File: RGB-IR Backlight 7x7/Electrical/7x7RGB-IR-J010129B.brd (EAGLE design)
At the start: 228.3 x 177.3 mm, 485 parts, among them P4 CON2X3, Q1 NPN_DUAL, Q10 NPN_DUAL, Q11 NPN_DUAL, Q12 NPN_DUAL, Q2 NPN_DUAL, Q3 NPN_DUAL, Q4 NPN_DUAL, Q5 NPN_DUAL, Q6 NPN_DUAL, Q7 NPN_DUAL, Q8 NPN_DUAL, Q9 NPN_DUAL, U1 AP8802, U2 AP8802, U3 AP8802, U4 AP8802

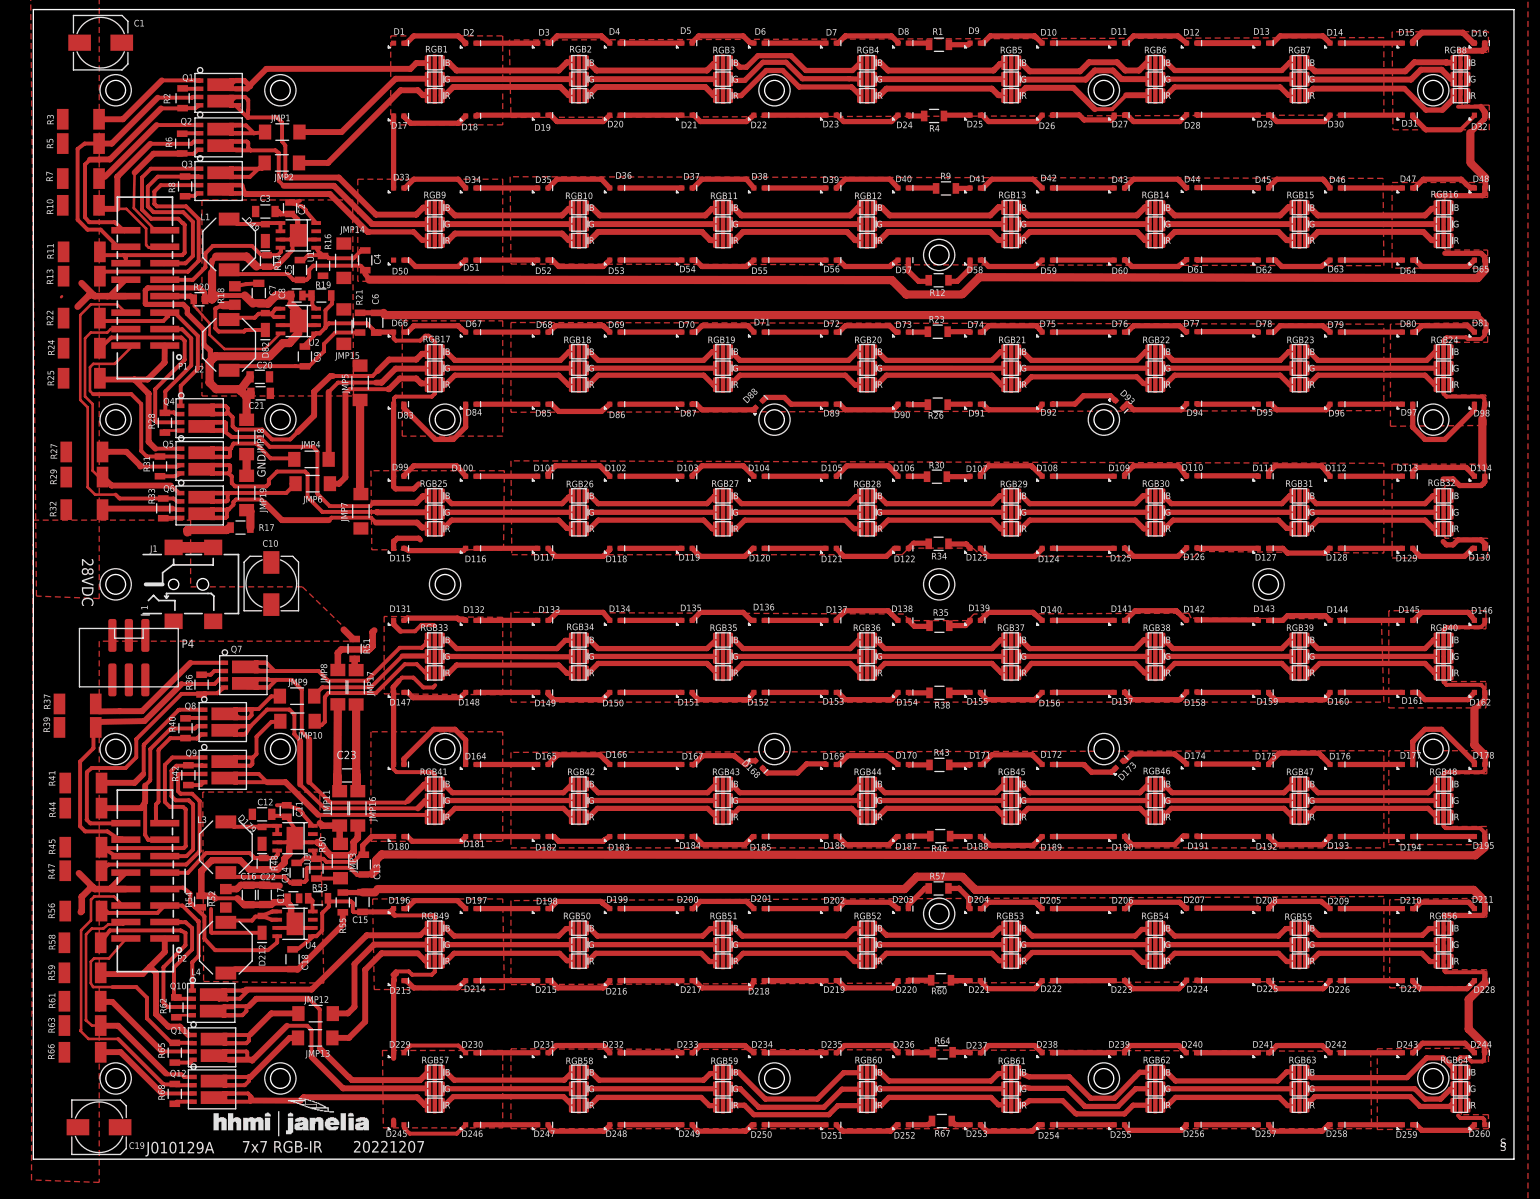
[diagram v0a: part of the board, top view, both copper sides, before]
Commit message: Add 7x7 RGB files
Add current PCB and cable assembly files for 7x7 RGB panel
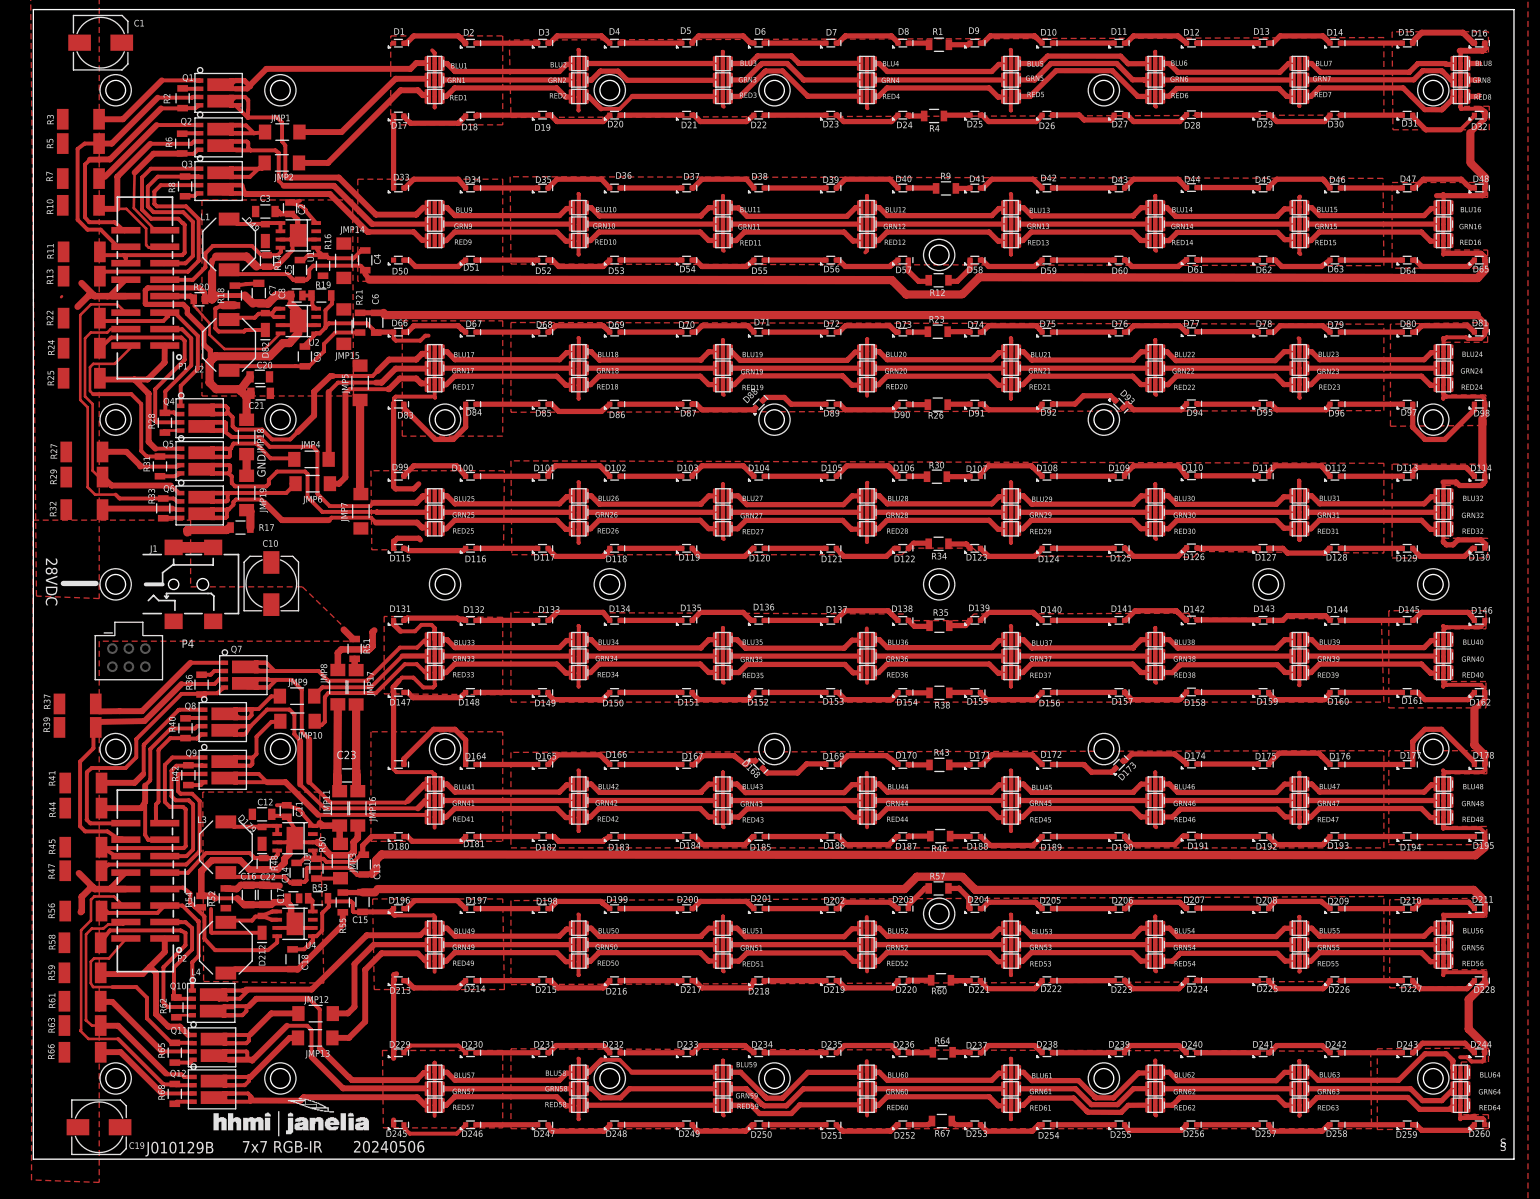
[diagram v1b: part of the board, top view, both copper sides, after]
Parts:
- removed RGB1, RGB10, RGB11, RGB12, RGB13, RGB14, RGB15, RGB16, RGB17, RGB18, RGB19, RGB2, RGB20, RGB21, RGB22, RGB23, RGB24, RGB25, RGB26, RGB27, RGB28, RGB29, RGB3, RGB30, RGB31, RGB32, RGB33, RGB34, RGB35, RGB36, RGB37, RGB38, RGB39, RGB4, RGB40, RGB41, RGB42, RGB43, RGB44, RGB45, RGB46, RGB47, RGB48, RGB49, RGB5, RGB50, RGB51, RGB52, RGB53, RGB54, RGB55, RGB56, RGB57, RGB58, RGB59, RGB6, RGB60, RGB61, RGB62, RGB63, RGB64, RGB7, RGB8, RGB9: LED_RGB_PADSUNPLUS, STEVES_BU:SUNPLUS_RGB
- added BLU1, BLU10, BLU11, BLU12, BLU13, BLU14, BLU15, BLU16, BLU17, BLU18, BLU19, BLU2, BLU20, BLU21, BLU22, BLU23, BLU24, BLU25, BLU26, BLU27, BLU28, BLU29, BLU3, BLU30, BLU31, BLU32, BLU33, BLU34, BLU35, BLU36, BLU37, BLU38, BLU39, BLU4, BLU40, BLU41, BLU42, BLU43, BLU44, BLU45, BLU46, BLU47, BLU48, BLU49, BLU5, BLU50, BLU51, BLU52, BLU53, BLU54, BLU55, BLU56, BLU57, BLU58, BLU59, BLU6, BLU60, BLU61, BLU62, BLU63, BLU64, BLU7, BLU8, BLU9: SP-BLU, RGB_IR_J010131revC:SUNPLUS-LED
- added GRN1, GRN10, GRN11, GRN12, GRN13, GRN14, GRN15, GRN16, GRN17, GRN18, GRN19, GRN2, GRN20, GRN21, GRN22, GRN23, GRN24, GRN25, GRN26, GRN27, GRN28, GRN29, GRN3, GRN30, GRN31, GRN32, GRN33, GRN34, GRN35, GRN36, GRN37, GRN38, GRN39, GRN4, GRN40, GRN41, GRN42, GRN43, GRN44, GRN45, GRN46, GRN47, GRN48, GRN49, GRN5, GRN50, GRN51, GRN52, GRN53, GRN54, GRN55, GRN56, GRN57, GRN58, GRN59, GRN6, GRN60, GRN61, GRN62, GRN63, GRN64, GRN7, GRN8, GRN9: SP-GRN, RGB_IR_J010131revC:SUNPLUS-LED
- added RED1, RED10, RED11, RED12, RED13, RED14, RED15, RED16, RED17, RED18, RED19, RED2, RED20, RED21, RED22, RED23, RED24, RED25, RED26, RED27, RED28, RED29, RED3, RED30, RED31, RED32, RED33, RED34, RED35, RED36, RED37, RED38, RED39, RED4, RED40, RED41, RED42, RED43, RED44, RED45, RED46, RED47, RED48, RED49, RED5, RED50, RED51, RED52, RED53, RED54, RED55, RED56, RED57, RED58, RED59, RED6, RED60, RED61, RED62, RED63, RED64, RED7, RED8, RED9: SP-RED, RGB_IR_J010131revC:SUNPLUS-LED
- added S29, S30, S31, S32: SCREW, STEVES_BU:4-40SOCKET
- P4: device STEVES_BU:2X3_SHROUDED_SMT -> STEVES_BU:2X3_PLUG
- R17, R21: value (none) -> 0R0
- R18, R52: device resistor:R1206 -> STEVES_BU:1206S
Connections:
- removed net N$343: C6.2, D114.C, D130.C, D81.C, D98.C, R21.2, RGB24.T, RGB32.T
- removed net N$413: RGB60.RA, RGB61.RC
- removed net N$417: RGB57.BA, RGB58.BC
- removed net N$418: RGB58.BA, RGB59.BC
- removed net N$419: RGB59.BA, RGB60.BC
- removed net N$420: RGB60.BA, RGB61.BC
- removed net N$421: RGB61.BA, RGB62.BC
- removed net N$422: RGB62.BA, RGB63.BC
- new net IR_RET2: BLU24.T, BLU32.T, C6.2, D114.C, D130.C, D81.C, D98.C, GRN24.T, GRN32.T, R21.2, RED24.T, RED32.T
- new net N$262: RED34.GA, RED35.GC
- new net N$267: RED33.GA, RED34.GC
- new net N$28: GRN5.GA, GRN6.GC
- new net N$292: BLU33.GA, BLU34.GC
- new net N$357: GRN46.GA, GRN47.GC
- new net N$403: RED61.GA, RED62.GC
- new net N$410: BLU59.GA, BLU60.GC
- net BLU1K: now also BLU1.GC; no longer RGB1.BC
- net BLU1K2: now also BLU9.GC; no longer RGB9.BC
- net BLU2K1: now also BLU17.GC; no longer RGB17.BC
- net BLU2K2: now also BLU25.GC; no longer RGB25.BC
- net BLU3K: now also BLU33.GC; no longer RGB33.BC
- net GRN1K: now also GRN1.GC; no longer RGB1.GC
- net GRN1K2: now also GRN9.GC; no longer RGB9.GC
- net GRN2K1: now also GRN17.GC; no longer RGB17.GC
- net GRN2K2: now also GRN25.GC; no longer RGB25.GC
- net GRN3K: now also GRN33.GC; no longer RGB33.GC
- net GULA_1: now also GRN57.GC; no longer RGB57.GC
- net GULA_2: now also RED57.GC; no longer RGB57.RC
- net GULA_3: now also GRN41.GC; no longer RGB41.GC
- net GULA_4: now also RED41.GC; no longer RGB41.RC
- net HS1: now also BLU2.T, BLU3.T, BLU4.T, BLU5.T, BLU6.T, BLU7.T, GRN2.T, GRN3.T, GRN4.T, GRN5.T, GRN6.T, GRN7.T, RED2.T, RED3.T, RED4.T, RED5.T, RED6.T, RED7.T; no longer RGB2.T, RGB3.T, RGB4.T, RGB5.T, RGB6.T, RGB7.T
- net HS2: now also BLU10.T, BLU11.T, BLU12.T, BLU13.T, BLU14.T, BLU15.T, GRN10.T, GRN11.T, GRN12.T, GRN13.T, GRN14.T, GRN15.T, RED10.T, RED11.T, RED12.T, RED13.T, RED14.T, RED15.T; no longer RGB10.T, RGB11.T, RGB12.T, RGB13.T, RGB14.T, RGB15.T
- net HS3: now also BLU18.T, BLU19.T, BLU20.T, BLU21.T, BLU22.T, BLU23.T, GRN18.T, GRN19.T, GRN20.T, GRN21.T, GRN22.T, GRN23.T, RED18.T, RED19.T, RED20.T, RED21.T, RED22.T, RED23.T; no longer RGB18.T, RGB19.T, RGB20.T, RGB21.T, RGB22.T, RGB23.T
- net HS4: now also BLU26.T, BLU27.T, BLU28.T, BLU29.T, BLU30.T, BLU31.T, GRN26.T, GRN27.T, GRN28.T, GRN29.T, GRN30.T, GRN31.T, RED26.T, RED27.T, RED28.T, RED29.T, RED30.T, RED31.T; no longer RGB26.T, RGB27.T, RGB28.T, RGB29.T, RGB30.T, RGB31.T
- net HS5: now also BLU34.T, BLU35.T, BLU36.T, BLU37.T, BLU38.T, BLU39.T, GRN34.T, GRN35.T, GRN36.T, GRN37.T, GRN38.T, GRN39.T, RED34.T, RED35.T, RED36.T, RED37.T, RED38.T, RED39.T; no longer RGB34.T, RGB35.T, RGB36.T, RGB37.T, RGB38.T, RGB39.T
- net HS6: now also BLU42.T, BLU43.T, BLU44.T, BLU45.T, BLU46.T, BLU47.T, GRN42.T, GRN43.T, GRN44.T, GRN45.T, GRN46.T, GRN47.T, RED42.T, RED43.T, RED44.T, RED45.T, RED46.T, RED47.T; no longer RGB42.T, RGB43.T, RGB44.T, RGB45.T, RGB46.T, RGB47.T
- net HS7: now also BLU50.T, BLU51.T, BLU52.T, BLU53.T, BLU54.T, BLU55.T, GRN50.T, GRN51.T, GRN52.T, GRN53.T, GRN54.T, GRN55.T, RED50.T, RED51.T, RED52.T, RED53.T, RED54.T, RED55.T; no longer RGB50.T, RGB51.T, RGB52.T, RGB53.T, RGB54.T, RGB55.T
- net HS8: now also BLU58.T, BLU59.T, BLU60.T, BLU61.T, BLU62.T, BLU63.T, GRN58.T, GRN59.T, GRN60.T, GRN61.T, GRN62.T, GRN63.T, RED58.T, RED59.T, RED60.T, RED61.T, RED62.T, RED63.T; no longer RGB58.T, RGB59.T, RGB60.T, RGB61.T, RGB62.T, RGB63.T
- net IR_DRV3: now also BLU33.T, BLU41.T, GRN33.T, GRN41.T, RED33.T, RED41.T; no longer RGB33.T, RGB41.T
- net IR_DRV4: now also BLU49.T, BLU57.T, GRN49.T, GRN57.T, RED49.T, RED57.T; no longer RGB49.T, RGB57.T
- net IR_DRV_UL1: now also BLU1.T, BLU9.T, GRN1.T, GRN9.T, RED1.T, RED9.T; no longer RGB1.T, RGB9.T
- net IR_DRV_UL2: now also BLU17.T, BLU25.T, GRN17.T, GRN25.T, RED17.T, RED25.T; no longer RGB17.T, RGB25.T
- net IR_RET3: now also BLU40.T, BLU48.T, GRN40.T, GRN48.T, RED40.T, RED48.T; no longer RGB40.T, RGB48.T
- net IR_RET_UL1: now also BLU16.T, BLU8.T, GRN16.T, GRN8.T, RED16.T, RED8.T; no longer RGB16.T, RGB8.T
- net I_RET4: now also BLU56.T, BLU64.T, GRN56.T, GRN64.T, RED56.T, RED64.T; no longer RGB56.T, RGB64.T
- net N$1: now also GRN10.GA, GRN11.GC; no longer RGB15.GA, RGB16.GC
- net N$100: now also BLU23.GA, BLU24.GC; no longer RGB17.RA, RGB18.RC
- net N$101: now also BLU19.GA, BLU20.GC; no longer RGB17.BA, RGB18.BC
- net N$102: now also RED19.GA, RED20.GC; no longer RGB18.BA, RGB19.BC
- net N$103: now also GRN19.GA, GRN20.GC; no longer RGB19.BA, RGB20.BC
- net N$104: now also GRN26.GA, GRN27.GC; no longer RGB20.BA, RGB21.BC
- net N$105: now also BLU22.GA, BLU23.GC; no longer RGB21.BA, RGB22.BC
- net N$106: now also RED22.GA, RED23.GC; no longer RGB22.BA, RGB23.BC
- net N$107: now also GRN22.GA, GRN23.GC; no longer RGB23.BA, RGB24.BC
- net N$12: now also RED10.GA, RED11.GC; no longer RGB13.GA, RGB14.GC
- net N$13: now also RED10.GC, RED9.GA; no longer RGB12.GA, RGB13.GC
- net N$135: now also GRN4.GA, GRN5.GC; no longer RGB7.GA, RGB8.GC
- net N$136: now also RED5.GA, RED6.GC; no longer RGB6.GA, RGB7.GC
- net N$137: now also RED4.GA, RED5.GC; no longer RGB5.GA, RGB6.GC
- net N$138: now also BLU4.GA, BLU5.GC; no longer RGB4.GA, RGB5.GC
- net N$139: now also BLU5.GA, BLU6.GC; no longer RGB3.GA, RGB4.GC
- net N$140: now also GRN2.GA, GRN3.GC; no longer RGB2.GA, RGB3.GC
- net N$141: now also GRN1.GA, GRN2.GC; no longer RGB1.GA, RGB2.GC
- net N$142: now also GRN7.GA, GRN8.GC; no longer RGB7.RA, RGB8.RC
- net N$143: now also RED7.GA, RED8.GC; no longer RGB6.RA, RGB7.RC
- net N$144: now also BLU7.GA, BLU8.GC; no longer RGB5.RA, RGB6.RC
- net N$145: now also BLU3.GA, BLU4.GC; no longer RGB4.RA, RGB5.RC
- net N$146: now also RED3.GA, RED4.GC; no longer RGB3.RA, RGB4.RC
- net N$147: now also RED2.GA, RED3.GC; no longer RGB2.RA, RGB3.RC
- net N$148: now also RED1.GA, RED2.GC; no longer RGB1.RA, RGB2.RC
- net N$149: now also BLU1.GA, BLU2.GC; no longer RGB1.BA, RGB2.BC
- net N$150: now also BLU2.GA, BLU3.GC; no longer RGB2.BA, RGB3.BC
- net N$151: now also GRN3.GA, GRN4.GC; no longer RGB3.BA, RGB4.BC
- net N$152: now also GRN14.GA, GRN15.GC; no longer RGB4.BA, RGB5.BC
- net N$153: now also BLU6.GA, BLU7.GC; no longer RGB5.BA, RGB6.BC
- net N$154: now also RED6.GA, RED7.GC; no longer RGB6.BA, RGB7.BC
- net N$155: now also GRN6.GA, GRN7.GC; no longer RGB7.BA, RGB8.BC
- net N$177: now also GRN41.GA, GRN42.GC; no longer RGB46.GA, RGB47.GC
- net N$178: now also RED42.GA, RED43.GC; no longer RGB45.GA, RGB46.GC
- net N$179: now also RED41.GA, RED42.GC; no longer RGB44.GA, RGB45.GC
- net N$181: now also BLU41.GA, BLU42.GC; no longer RGB43.GA, RGB44.GC
- net N$188: now also BLU42.GA, BLU43.GC; no longer RGB42.GA, RGB43.GC
- net N$190: now also RED58.GA, RED59.GC; no longer RGB63.GA, RGB64.GC
- net N$191: now also GRN25.GA, GRN26.GC; no longer RGB31.GA, RGB32.GC
- net N$192: now also RED26.GA, RED27.GC; no longer RGB30.GA, RGB31.GC
- net N$193: now also RED25.GA, RED26.GC; no longer RGB29.GA, RGB30.GC
- net N$194: now also BLU25.GA, BLU26.GC; no longer RGB28.GA, RGB29.GC
- net N$195: now also BLU26.GA, BLU27.GC; no longer RGB27.GA, RGB28.GC
- net N$196: now also GRN29.GA, GRN30.GC; no longer RGB26.GA, RGB27.GC
- net N$197: now also GRN28.GA, GRN29.GC; no longer RGB25.GA, RGB26.GC
- net N$198: now also RED29.GA, RED30.GC; no longer RGB31.RA, RGB32.RC
- net N$199: now also RED28.GA, RED29.GC; no longer RGB30.RA, RGB31.RC
- net N$20: now also RED49.GC; no longer RGB49.RC
- net N$200: now also BLU28.GA, BLU29.GC; no longer RGB29.RA, RGB30.RC
- net N$201: now also BLU29.GA, BLU30.GC; no longer RGB28.RA, RGB29.RC
- net N$202: now also GRN31.GA, GRN32.GC; no longer RGB27.RA, RGB28.RC
- net N$203: now also RED31.GA, RED32.GC; no longer RGB26.RA, RGB27.RC
- net N$204: now also BLU31.GA, BLU32.GC; no longer RGB25.RA, RGB26.RC
- net N$205: now also BLU27.GA, BLU28.GC; no longer RGB25.BA, RGB26.BC
- net N$206: now also RED27.GA, RED28.GC; no longer RGB26.BA, RGB27.BC
- net N$207: now also GRN27.GA, GRN28.GC; no longer RGB27.BA, RGB28.BC
- net N$208: now also GRN34.GA, GRN35.GC; no longer RGB28.BA, RGB29.BC
- net N$209: now also BLU30.GA, BLU31.GC; no longer RGB29.BA, RGB30.BC
- net N$210: now also RED30.GA, RED31.GC; no longer RGB30.BA, RGB31.BC
- net N$211: now also GRN30.GA, GRN31.GC; no longer RGB31.BA, RGB32.BC
- net N$230: now also GRN45.GA, GRN46.GC; no longer RGB41.GA, RGB42.GC
- net N$233: now also GRN44.GA, GRN45.GC; no longer RGB47.RA, RGB48.RC
- net N$235: now also RED45.GA, RED46.GC; no longer RGB46.RA, RGB47.RC
- net N$238: now also RED44.GA, RED45.GC; no longer RGB45.RA, RGB46.RC
- net N$239: now also BLU44.GA, BLU45.GC; no longer RGB44.RA, RGB45.RC
- net N$240: now also BLU45.GA, BLU46.GC; no longer RGB43.RA, RGB44.RC
- net N$241: now also GRN47.GA, GRN48.GC; no longer RGB42.RA, RGB43.RC
- net N$242: now also RED47.GA, RED48.GC; no longer RGB41.RA, RGB42.RC
- net N$243: now also BLU47.GA, BLU48.GC; no longer RGB41.BA, RGB42.BC
- net N$244: now also BLU43.GA, BLU44.GC; no longer RGB42.BA, RGB43.BC
- net N$245: now also RED43.GA, RED44.GC; no longer RGB43.BA, RGB44.BC
- net N$248: now also GRN43.GA, GRN44.GC; no longer RGB44.BA, RGB45.BC
- net N$249: now also GRN50.GA, GRN51.GC; no longer RGB45.BA, RGB46.BC
- net N$250: now also BLU46.GA, BLU47.GC; no longer RGB46.BA, RGB47.BC
- net N$251: now also RED46.GA, RED47.GC; no longer RGB47.BA, RGB48.BC
- net N$26: now also GRN58.GA, GRN59.GC; no longer RGB63.BA, RGB64.BC
- net N$261: now also GRN33.GA, GRN34.GC; no longer RGB33.RA, RGB34.RC
- net N$294: now also GRN49.GA, GRN50.GC; no longer RGB55.GA, RGB56.GC
- net N$295: now also RED50.GA, RED51.GC; no longer RGB54.GA, RGB55.GC
- net N$296: now also RED49.GA, RED50.GC; no longer RGB53.GA, RGB54.GC
- net N$297: now also BLU49.GA, BLU50.GC; no longer RGB52.GA, RGB53.GC
- net N$298: now also BLU50.GA, BLU51.GC; no longer RGB51.GA, RGB52.GC
- net N$299: now also GRN53.GA, GRN54.GC; no longer RGB50.GA, RGB51.GC
- net N$30: now also GRN57.GA, GRN58.GC; no longer RGB63.RA, RGB64.RC
- net N$300: now also GRN52.GA, GRN53.GC; no longer RGB49.GA, RGB50.GC
- net N$301: now also RED53.GA, RED54.GC; no longer RGB55.RA, RGB56.RC
- net N$302: now also RED52.GA, RED53.GC; no longer RGB54.RA, RGB55.RC
- net N$303: now also BLU52.GA, BLU53.GC; no longer RGB53.RA, RGB54.RC
- net N$304: now also BLU53.GA, BLU54.GC; no longer RGB52.RA, RGB53.RC
- net N$305: now also GRN55.GA, GRN56.GC; no longer RGB51.RA, RGB52.RC
- net N$306: now also RED55.GA, RED56.GC; no longer RGB50.RA, RGB51.RC
- net N$307: now also BLU55.GA, BLU56.GC; no longer RGB49.RA, RGB50.RC
- net N$308: now also BLU51.GA, BLU52.GC; no longer RGB49.BA, RGB50.BC
- net N$309: now also RED51.GA, RED52.GC; no longer RGB50.BA, RGB51.BC
- net N$310: now also GRN51.GA, GRN52.GC; no longer RGB51.BA, RGB52.BC
- net N$311: now also RED57.GA, RED58.GC; no longer RGB52.BA, RGB53.BC
- net N$312: now also BLU54.GA, BLU55.GC; no longer RGB53.BA, RGB54.BC
- net N$313: now also RED54.GA, RED55.GC; no longer RGB54.BA, RGB55.BC
- net N$314: now also GRN54.GA, GRN55.GC; no longer RGB55.BA, RGB56.BC
- net N$344: now also BLU34.GA, BLU35.GC; no longer RGB39.GA, RGB40.GC
- net N$345: now also GRN37.GA, GRN38.GC; no longer RGB38.GA, RGB39.GC
- net N$346: now also GRN36.GA, GRN37.GC; no longer RGB37.GA, RGB38.GC
- net N$347: now also RED37.GA, RED38.GC; no longer RGB36.GA, RGB37.GC
- net N$348: now also RED36.GA, RED37.GC; no longer RGB35.GA, RGB36.GC
- net N$349: now also BLU36.GA, BLU37.GC; no longer RGB34.GA, RGB35.GC
- net N$350: now also BLU37.GA, BLU38.GC; no longer RGB33.GA, RGB34.GC
- net N$351: now also GRN39.GA, GRN40.GC; no longer RGB39.RA, RGB40.RC
- net N$352: now also RED39.GA, RED40.GC; no longer RGB38.RA, RGB39.RC
- net N$353: now also BLU39.GA, BLU40.GC; no longer RGB37.RA, RGB38.RC
- net N$354: now also BLU35.GA, BLU36.GC; no longer RGB36.RA, RGB37.RC
- net N$355: now also RED35.GA, RED36.GC; no longer RGB35.RA, RGB36.RC
- net N$356: now also GRN35.GA, GRN36.GC; no longer RGB34.RA, RGB35.RC
- net N$358: now also BLU38.GA, BLU39.GC; no longer RGB33.BA, RGB34.BC
- net N$359: now also RED38.GA, RED39.GC; no longer RGB34.BA, RGB35.BC
- net N$360: now also GRN38.GA, GRN39.GC; no longer RGB35.BA, RGB36.BC
- net N$361: now also BLU57.GA, BLU58.GC; no longer RGB36.BA, RGB37.BC
- net N$362: now also BLU58.GA, BLU59.GC; no longer RGB37.BA, RGB38.BC
- net N$363: now also GRN61.GA, GRN62.GC; no longer RGB38.BA, RGB39.BC
- net N$364: now also GRN60.GA, GRN61.GC; no longer RGB39.BA, RGB40.BC
- net N$40: now also BLU10.GC, BLU9.GA; no longer RGB11.GA, RGB12.GC
- net N$401: now also BLU41.GC; no longer RGB41.BC
- net N$404: now also RED60.GA, RED61.GC; no longer RGB62.GA, RGB63.GC
- net N$405: now also BLU60.GA, BLU61.GC; no longer RGB61.GA, RGB62.GC
- net N$406: now also BLU61.GA, BLU62.GC; no longer RGB60.GA, RGB61.GC
- net N$407: now also GRN63.GA, GRN64.GC; no longer RGB59.GA, RGB60.GC
- net N$408: now also RED63.GA, RED64.GC; no longer RGB58.GA, RGB59.GC
- net N$409: now also BLU63.GA, BLU64.GC; no longer RGB57.GA, RGB58.GC
- net N$41: now also BLU10.GA, BLU11.GC; no longer RGB10.GA, RGB11.GC
- net N$411: now also RED59.GA, RED60.GC; no longer RGB62.RA, RGB63.RC
- net N$412: now also GRN59.GA, GRN60.GC; no longer RGB61.RA, RGB62.RC
- net N$414: now also BLU62.GA, BLU63.GC; no longer RGB59.RA, RGB60.RC
- net N$415: now also RED62.GA, RED63.GC; no longer RGB58.RA, RGB59.RC
- net N$416: now also GRN62.GA, GRN63.GC; no longer RGB57.RA, RGB58.RC
- net N$42: now also GRN13.GA, GRN14.GC; no longer RGB10.GC, RGB9.GA
- net N$43: now also GRN12.GA, GRN13.GC; no longer RGB15.RA, RGB16.RC
- net N$44: now also RED13.GA, RED14.GC; no longer RGB14.RA, RGB15.RC
- net N$45: now also RED12.GA, RED13.GC; no longer RGB13.RA, RGB14.RC
- net N$46: now also BLU12.GA, BLU13.GC; no longer RGB12.RA, RGB13.RC
- net N$47: now also BLU13.GA, BLU14.GC; no longer RGB11.RA, RGB12.RC
- net N$48: now also GRN15.GA, GRN16.GC; no longer RGB10.RA, RGB11.RC
- net N$49: now also RED15.GA, RED16.GC; no longer RGB10.RC, RGB9.RA
- net N$5: now also GRN49.GC; no longer RGB49.GC
- net N$50: now also BLU15.GA, BLU16.GC; no longer RGB10.BC, RGB9.BA
- net N$51: now also BLU11.GA, BLU12.GC; no longer RGB10.BA, RGB11.BC
- net N$52: now also RED11.GA, RED12.GC; no longer RGB11.BA, RGB12.BC
- net N$53: now also GRN11.GA, GRN12.GC; no longer RGB12.BA, RGB13.BC
- net N$54: now also GRN18.GA, GRN19.GC; no longer RGB13.BA, RGB14.BC
- net N$55: now also BLU14.GA, BLU15.GC; no longer RGB14.BA, RGB15.BC
- net N$56: now also RED14.GA, RED15.GC; no longer RGB15.BA, RGB16.BC
- net N$6: now also BLU49.GC; no longer RGB49.BC
- net N$7: now also GRN10.GC, GRN9.GA; no longer RGB14.GA, RGB15.GC
- net N$8: now also BLU57.GC; no longer RGB57.BC
- net N$86: now also GRN17.GA, GRN18.GC; no longer RGB23.GA, RGB24.GC
- net N$87: now also RED18.GA, RED19.GC; no longer RGB22.GA, RGB23.GC
- net N$88: now also RED17.GA, RED18.GC; no longer RGB21.GA, RGB22.GC
- net N$89: now also BLU17.GA, BLU18.GC; no longer RGB20.GA, RGB21.GC
- net N$90: now also BLU18.GA, BLU19.GC; no longer RGB19.GA, RGB20.GC
- net N$91: now also GRN21.GA, GRN22.GC; no longer RGB18.GA, RGB19.GC
- net N$92: now also GRN20.GA, GRN21.GC; no longer RGB17.GA, RGB18.GC
- net N$93: now also RED21.GA, RED22.GC; no longer RGB23.RA, RGB24.RC
- net N$94: now also RED20.GA, RED21.GC; no longer RGB22.RA, RGB23.RC
- net N$95: now also BLU20.GA, BLU21.GC; no longer RGB21.RA, RGB22.RC
- net N$96: now also BLU21.GA, BLU22.GC; no longer RGB20.RA, RGB21.RC
- net N$97: now also GRN42.GA, GRN43.GC; no longer RGB47.GA, RGB48.GC
- net N$98: now also GRN23.GA, GRN24.GC; no longer RGB19.RA, RGB20.RC
- net N$99: now also RED23.GA, RED24.GC; no longer RGB18.RA, RGB19.RC
- net RED1K: now also RED1.GC; no longer RGB1.RC
- net RED1K2: now also RED9.GC; no longer RGB9.RC
- net RED2K1: now also RED17.GC; no longer RGB17.RC
- net RED2K2: now also RED25.GC; no longer RGB25.RC
- net RED3K: now also RED33.GC; no longer RGB33.RC
- net V_RGB: now also BLU16.GA, BLU24.GA, BLU32.GA, BLU40.GA, BLU48.GA, BLU56.GA, BLU64.GA, BLU8.GA, GRN16.GA, GRN24.GA, GRN32.GA, GRN40.GA, GRN48.GA, GRN56.GA, GRN64.GA, GRN8.GA, RED16.GA, RED24.GA, RED32.GA, RED40.GA, RED48.GA, RED56.GA, RED64.GA, RED8.GA; no longer RGB16.BA, RGB16.GA, RGB16.RA, RGB24.BA, RGB24.GA, RGB24.RA, RGB32.BA, RGB32.GA, RGB32.RA, RGB40.BA, RGB40.GA, RGB40.RA, RGB48.BA, RGB48.GA, RGB48.RA, RGB56.BA, RGB56.GA, RGB56.RA, RGB64.BA, RGB64.GA, RGB64.RA, RGB8.BA, RGB8.GA, RGB8.RA
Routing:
- net IR_RET2: track 0.00 -> 236.5 mm
- net N$343: track 224.4 -> 0.00 mm
- net HS4: track 0.00 -> 58.6 mm
- net HS2: track 0.00 -> 54.1 mm
- net HS3: track 0.00 -> 53.4 mm
- net HS8: track 0.00 -> 52.9 mm
- net HS7: track 0.00 -> 52.9 mm
- net HS6: track 0.00 -> 52.9 mm
- net HS5: track 0.00 -> 51.4 mm
- net HS1: track 0.00 -> 49.5 mm
- net N$419: track 23.5 -> 0.00 mm
- net N$410: track 0.00 -> 23.5 mm
- net N$421: track 23.3 -> 0.00 mm
- net N$28: track 0.00 -> 22.3 mm
- net N$403: track 0.00 -> 21.9 mm
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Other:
- board text added: "20240506"
- board text added: "J010129B"
- board text removed: "20221207"
- board text removed: "J010129A"
